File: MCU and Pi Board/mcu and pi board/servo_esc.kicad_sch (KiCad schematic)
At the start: 4 parts, among them J10 Conn_01x03_Pin, J11 Conn_01x03_Pin, J8 PWM Connector, J9 Conn_01x03_Pin

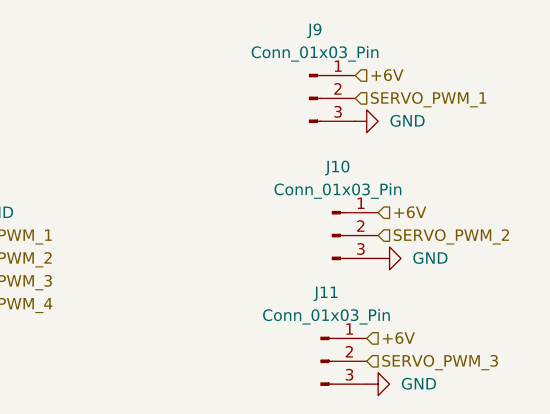
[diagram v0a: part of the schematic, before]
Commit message: added leds and minor fixes
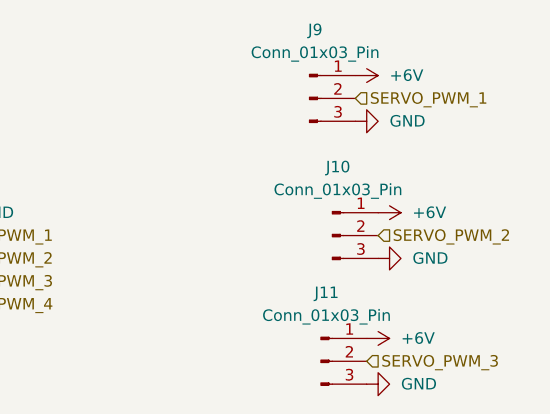
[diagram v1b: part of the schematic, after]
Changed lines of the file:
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@@
-		)
-	)
-	(hierarchical_label "+6V"
-		(shape input)
-		(at 165.1 49.53 0)
-		(effects
-			(font
-				(size 1.27 1.27)
-			)
-			(justify left)
 		)
 	)
@@
 		)
 	)
-	(hierarchical_label "+6V"
-		(shape input)
-		(at 167.64 64.77 0)
-		(effects
-			(font
-				(size 1.27 1.27)
-			)
-			(justify left)
-		)
-	)
 	(hierarchical_label "ESC_PWM_2"
 		(shape input)
@@
 		)
 	)
-	(hierarchical_label "+6V"
-		(shape input)
-		(at 166.37 78.74 0)
-		(effects
-			(font
-				(size 1.27 1.27)
-			)
-			(justify left)
-		)
-	)
 	(hierarchical_label "ESC_PWM_1"
 		(shape input)
@@
 	)
 	(symbol
+		(lib_id "power:+6V")
+		(at 165.1 49.53 270)
+		(unit 1)
+		(exclude_from_sim no)
+		(in_bom yes)
+		(on_board yes)
+		(dnp no)
+		(fields_autoplaced yes)
+		(property "Reference" "#PWR062"
+			(at 161.29 49.53 0)
+			(effects
+				(font
+					(size 1.27 1.27)
+				)
+				(hide yes)
+			)
+		)
+		(property "Value" "+6V"
+			(at 168.91 49.5299 90)
+			(effects
+				(font
+					(size 1.27 1.27)
+				)
+				(justify left)
+			)
+		)
+		(property "Footprint" ""
+			(at 165.1 49.53 0)
+			(effects
+				(font
+					(size 1.27 1.27)
+				)
+				(hide yes)
+			)
+		)
+		(property "Datasheet" ""
+			(at 165.1 49.53 0)
+			(effects
+				(font
+					(size 1.27 1.27)
+				)
+				(hide yes)
+			)
+		)
+		(property "Description" "Power symbol creates a global label with name \"+6V\""
+			(at 165.1 49.53 0)
+			(effects
+				(font
+					(size 1.27 1.27)
+				)
+				(hide yes)
+			)
+		)
+		(pin "1"
+		)
+		(instances
+			(project ""
+				(path "/b20a486a-db1b-4621-abfe-a5d205c676b3/cf9b13c4-ce92-4bbb-82dc-82851d7b76da"
+					(reference "#PWR062")
+					(unit 1)
+				)
+			)
+		)
+	)
+	(symbol
 		(lib_id "power:GND")
 		(at 93.98 67.31 270)
@@
 	)
 	(symbol
+		(lib_id "power:+6V")
+		(at 167.64 64.77 270)
+		(unit 1)
+		(exclude_from_sim no)
+		(in_bom yes)
+		(on_board yes)
+		(dnp no)
+		(fields_autoplaced yes)
+		(property "Reference" "#PWR063"
+			(at 163.83 64.77 0)
+			(effects
+				(font
+					(size 1.27 1.27)
+				)
+				(hide yes)
+			)
+		)
+		(property "Value" "+6V"
+			(at 171.45 64.7699 90)
+			(effects
+				(font
+					(size 1.27 1.27)
+				)
+				(justify left)
+			)
+		)
+		(property "Footprint" ""
+			(at 167.64 64.77 0)
+			(effects
+				(font
+					(size 1.27 1.27)
+				)
+				(hide yes)
+			)
+		)
+		(property "Datasheet" ""
+			(at 167.64 64.77 0)
+			(effects
+				(font
+					(size 1.27 1.27)
+				)
+				(hide yes)
+			)
+		)
+		(property "Description" "Power symbol creates a global label with name \"+6V\""
+			(at 167.64 64.77 0)
+			(effects
+				(font
+					(size 1.27 1.27)
+				)
+				(hide yes)
+			)
+		)
+		(pin "1"
+		)
+		(instances
+			(project "mcu and pi board"
+				(path "/b20a486a-db1b-4621-abfe-a5d205c676b3/cf9b13c4-ce92-4bbb-82dc-82851d7b76da"
+					(reference "#PWR063")
+					(unit 1)
+				)
+			)
+		)
+	)
+	(symbol
 		(lib_id "Connector:Conn_01x03_Pin")
 		(at 161.29 81.28 0)
@@
 					(unit 1)
 				)
+			)
+		)
+	)
+	(symbol
+		(lib_id "power:+6V")
+		(at 166.37 78.74 270)
+		(unit 1)
+		(exclude_from_sim no)
+		(in_bom yes)
+		(on_board yes)
+		(dnp no)
+		(fields_autoplaced yes)
+		(property "Reference" "#PWR064"
+			(at 162.56 78.74 0)
+			(effects
+				(font
+					(size 1.27 1.27)
+				)
+				(hide yes)
+			)
+		)
+		(property "Value" "+6V"
+			(at 170.18 78.7399 90)
+			(effects
+				(font
+					(size 1.27 1.27)
+				)
+				(justify left)
+			)
+		)
+		(property "Footprint" ""
+			(at 166.37 78.74 0)
+			(effects
+				(font
+					(size 1.27 1.27)
+				)
+				(hide yes)
+			)
+		)
+		(property "Datasheet" ""
+			(at 166.37 78.74 0)
+			(effects
+				(font
+					(size 1.27 1.27)
+				)
+				(hide yes)
+			)
+		)
+		(property "Description" "Power symbol creates a global label with name \"+6V\""
+			(at 166.37 78.74 0)
+			(effects
+				(font
+					(size 1.27 1.27)
+				)
+				(hide yes)
+			)
+		)
+		(pin "1"
+		)
+		(instances
+			(project "mcu and pi board"
+				(path "/b20a486a-db1b-4621-abfe-a5d205c676b3/cf9b13c4-ce92-4bbb-82dc-82851d7b76da"
+					(reference "#PWR064")
+					(unit 1)
+				)

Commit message: minor edits
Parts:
- added C8: 10u, symbol Device:C
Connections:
- net +12V: now also C8.1
- net GND: now also C8.2
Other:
- note added: "Add decoupling to servos"
- note added: "Add decoupling to thrusters"
- note added: "add tools c"
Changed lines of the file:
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@@
 	(generator_version "9.0")
 	(paper "A4")
+	(text "Add decoupling to servos"
+		(exclude_from_sim no)
+		(at 192.278 56.388 0)
+		(effects
+			(font
+				(size 1.27 1.27)
+			)
+		)
+	)
+	(text "add tools c"
+		(exclude_from_sim no)
+		(at 102.616 83.312 0)
+		(effects
+			(font
+				(size 1.27 1.27)
+			)
+		)
+	)
+	(text "Add decoupling to thrusters\n"
+		(exclude_from_sim no)
+		(at 104.648 53.848 0)
+		(effects
+			(font
+				(size 1.27 1.27)
+			)
+		)
+	)
+	(junction
+		(at 83.82 59.69)
+		(diameter 0)
+		(color 0 0 0 0)
+	)
+	(junction
+		(at 83.82 67.31)
+		(diameter 0)
+		(color 0 0 0 0)
+	)
+	(wire
+		(pts
+			(xy 91.44 59.69) (xy 91.44 64.77)
+		)
+		(stroke
+			(width 0)
+			(type default)
+		)
+	)
+	(wire
+		(pts
+			(xy 91.44 64.77) (xy 93.98 64.77)
+		)
+		(stroke
+			(width 0)
+			(type default)
+		)
+	)
+	(wire
+		(pts
+			(xy 82.55 67.31) (xy 83.82 67.31)
+		)
+		(stroke
+			(width 0)
+			(type default)
+		)
+	)
+	(wire
+		(pts
+			(xy 83.82 67.31) (xy 93.98 67.31)
+		)
+		(stroke
+			(width 0)
+			(type default)
+		)
+	)
+	(wire
+		(pts
+			(xy 83.82 59.69) (xy 91.44 59.69)
+		)
+		(stroke
+			(width 0)
+			(type default)
+		)
+	)
+	(wire
+		(pts
+			(xy 82.55 59.69) (xy 83.82 59.69)
+		)
+		(stroke
+			(width 0)
+			(type default)
+		)
+	)
 	(hierarchical_label "SERVO_PWM_3"
 		(shape input)
@@
 	(symbol
 		(lib_id "power:GND")
-		(at 93.98 67.31 270)
+		(at 82.55 67.31 270)
 		(unit 1)
 		(exclude_from_sim no)
@@
 		(fields_autoplaced yes)
 		(property "Reference" "#PWR032"
-			(at 87.63 67.31 0)
+			(at 76.2 67.31 0)
 			(effects
 				(font
@@
 		)
 		(property "Value" "GND"
-			(at 90.17 67.3099 90)
+			(at 78.74 67.3099 90)
 			(effects
 				(font
@@
 		)
 		(property "Footprint" ""
-			(at 93.98 67.31 0)
+			(at 82.55 67.31 0)
 			(effects
 				(font
@@
 		)
 		(property "Datasheet" ""
-			(at 93.98 67.31 0)
+			(at 82.55 67.31 0)
 			(effects
 				(font
@@
 		)
 		(property "Description" "Power symbol creates a global label with name \"GND\" , ground"
-			(at 93.98 67.31 0)
+			(at 82.55 67.31 0)
 			(effects
 				(font
@@
 	(symbol
 		(lib_id "power:+12V")
-		(at 93.98 64.77 90)
+		(at 82.55 59.69 90)
 		(unit 1)
 		(exclude_from_sim no)
@@
 		(fields_autoplaced yes)
 		(property "Reference" "#PWR031"
-			(at 97.79 64.77 0)
+			(at 86.36 59.69 0)
 			(effects
 				(font
@@
 		)
 		(property "Value" "+12V"
-			(at 90.17 64.7699 90)
+			(at 78.74 59.6899 90)
 			(effects
 				(font
@@
 		)
 		(property "Footprint" ""
-			(at 93.98 64.77 0)
+			(at 82.55 59.69 0)
 			(effects
 				(font
@@
 		)
 		(property "Datasheet" ""
-			(at 93.98 64.77 0)
+			(at 82.55 59.69 0)
 			(effects
 				(font
@@
 		)
 		(property "Description" "Power symbol creates a global label with name \"+12V\""
-			(at 93.98 64.77 0)
+			(at 82.55 59.69 0)
 			(effects
 				(font
@@
 					(unit 1)
 				)
+			)
+		)
+	)
+	(symbol
+		(lib_id "Device:C")
+		(at 83.82 63.5 0)
+		(unit 1)
+		(exclude_from_sim no)
+		(in_bom yes)
+		(on_board yes)
+		(dnp no)
+		(fields_autoplaced yes)
+		(property "Reference" "C8"
+			(at 87.63 62.2299 0)
+			(effects
+				(font
+					(size 1.27 1.27)
+				)
+				(justify left)
+			)
+		)
+		(property "Value" "10u"
+			(at 87.63 64.7699 0)
+			(effects
+				(font
+					(size 1.27 1.27)
+				)
+				(justify left)
+			)
+		)
+		(property "Footprint" ""
+			(at 84.7852 67.31 0)
+			(effects
+				(font
+					(size 1.27 1.27)
+				)
+				(hide yes)
+			)
+		)
+		(property "Datasheet" "~"
+			(at 83.82 63.5 0)
+			(effects
+				(font
+					(size 1.27 1.27)
+				)
+				(hide yes)
+			)
+		)
+		(property "Description" "Unpolarized capacitor"
+			(at 83.82 63.5 0)
+			(effects
+				(font
+					(size 1.27 1.27)
+				)
+				(hide yes)
+			)
+		)
+		(pin "1"
+		)
+		(pin "2"
+		)
+		(instances
+			(project ""
+				(path "/b20a486a-db1b-4621-abfe-a5d205c676b3/cf9b13c4-ce92-4bbb-82dc-82851d7b76da"
+					(reference "C8")
+					(unit 1)
+				)

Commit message: pretty much done i think
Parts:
- added C10, C22, C23, C24, C25: 1000u, symbol Device:C
- added C17: 1u, symbol Device:C
- added C20, C21, C9: 0.1u, symbol Device:C
- added R10, R17, R9: 100, symbol Device:R_US
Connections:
- net +12V: now also C23.1, C24.1, C25.1
- net +6V: now also C10.1, C17.1, C22.1
- net GND: now also C10.2, C17.2, C20.2, C21.2, C22.2, C23.2, C24.2, C25.2, C9.2
- net SERVO_PWM_1: now also R9.2; no longer J9.2 (Pin_2)
- net SERVO_PWM_2: now also R10.2; no longer J10.2 (Pin_2)
- net SERVO_PWM_3: now also R17.2; no longer J11.2 (Pin_2)
- new net: C20.1, J10.2 (Pin_2), R10.1
- new net: C21.1, J11.2 (Pin_2), R17.1
- new net: C9.1, J9.2 (Pin_2), R9.1
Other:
- note added: "buffer current spikes"
- note added: "filter high frequency"
- note removed: "add tools c"
- moved on the sheet: C8, J10, J11, J9

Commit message: pretty much done
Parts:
- added J22: Conn_01x03_Pin, symbol Connector:Conn_01x03_Pin
- added U6, U7: MC74HC157ADR2G, SOIC-16_ONS, symbol custom library:MC74HC157ADR2G
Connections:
- net SERVO_PWM_3 is gone; now on net SERVO_PWM_2: R17.2
- net +5V: now also J22.1 (Pin_1), U6.16 (VCC), U7.16 (VCC)
- net ESC_PWM_1: now also U6.7 (Y1)
- net ESC_PWM_2: now also U6.9 (Y2)
- net ESC_PWM_3: now also U6.12 (Y3)
- net GND: now also J22.3 (Pin_3), U6.15 (OUTPUTENABLE), U6.8 (GND), U7.15 (OUTPUTENABLE), U7.8 (GND)
- net SERVO_PWM_1: now also R10.2, U7.7 (Y1); no longer R9.2
- net SERVO_PWM_2: now also U7.9 (Y2); no longer R10.2
- new net ESC_PWM_0: U6.4 (Y0)
- new net RP2350B_ESC_PWM_0: U6.3 (B0)
- new net RP2350B_ESC_PWM_1: U6.6 (B1)
- new net RP2350B_ESC_PWM_2: U6.10 (B2)
- new net RP2350B_ESC_PWM_3: U6.13 (B3)
- new net RP2350B_SERVO_PWM_0: U7.3 (B0)
- new net RP2350B_SERVO_PWM_1: U7.6 (B1)
- new net RP2350B_SERVO_PWM_2: U7.10 (B2)
- new net SEL: J22.2 (Pin_2), U6.1 (SELECT), U7.1 (SELECT)
- new net SERVO_PWM_0: R9.2, U7.4 (Y0)
- new net STM_ESC_PWM_0: U6.2 (A0)
- new net STM_ESC_PWM_1: U6.5 (A1)
- new net STM_ESC_PWM_2: U6.11 (A2)
- new net STM_ESC_PWM_3: U6.14 (A3)
- new net STM_SERVO_PWM_0: U7.2 (A0)
- new net STM_SERVO_PWM_1: U7.5 (A1)
- new net STM_SERVO_PWM_2: U7.11 (A2)
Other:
- note removed: "Add decoupling to servos"
- note removed: "Add decoupling to thrusters"

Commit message: started routing
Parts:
- removed C10: 1000u, symbol Device:C
- removed C20, C21, C9: 0.1u, symbol Device:C
- removed J10, J11, J9: Conn_01x03_Pin, symbol Connector:Conn_01x03_Pin
- removed R10, R17, R9: 100, symbol Device:R_US
- added C26, C39: 0.1u, Capacitor_SMD:C_0603_1608Metric_Pad1.08x0.95mm_HandSolder, symbol Device:C
- added C27, C40: 10u, Capacitor_SMD:C_0805_2012Metric_Pad1.18x1.45mm_HandSolder, symbol Device:C
- added J23, J24, J25: TB006-508-03BE, custom library:CUI_TB006-508-03BE, symbol custom library:TB006-508-03BE
- added J9: ESC ADAPTER - BACKPLANE, custom library:ESC Adapter - Backplane, symbol custom library:IPBT-105-H1-T-D-GP
- C17: value 1u -> 0.1u; footprint (none) -> Capacitor_SMD:C_0603_1608Metric_Pad1.08x0.95mm_HandSolder
- C22, C24: value 1000u -> 10u; footprint (none) -> Capacitor_SMD:C_0805_2012Metric_Pad1.18x1.45mm_HandSolder
- C23, C25: value 1000u -> 0.1u; footprint (none) -> Capacitor_SMD:C_0603_1608Metric_Pad1.08x0.95mm_HandSolder
- C8: footprint (none) -> Capacitor_SMD:C_0805_2012Metric_Pad1.18x1.45mm_HandSolder
- J22: footprint (none) -> Connector_PinHeader_2.54mm:PinHeader_1x03_P2.54mm_Vertical
- J8: footprint Custom:PWM, 12V, GND JST Connector -> custom library:PWM, 12V, GND JST Connector
- U6, U7: footprint SOIC-16_ONS -> custom library:SOIC-16_ONS
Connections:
- net ESC_PWM_0 is gone; now on net ESC_PWM_1: U6.4 (Y0)
- net +12V: now also C26.1, J9.04, J9.05, J9.09, J9.10, J9.11, J9.21, J9.22, J9.23, J9.26, J9.27, J9.28; no longer C25.1
- net +5V: now also J9.12
- net +6V: now also C25.1, C27.1, C39.1, C40.1, J23.1, J24.1, J25.1
- net ESC_PWM_1: now also J9.16; no longer U6.7 (Y1)
- net ESC_PWM_2: now also U6.7 (Y1), J9.19; no longer U6.9 (Y2)
- net ESC_PWM_3: now also U6.9 (Y2), J9.15; no longer U6.12 (Y3)
- net ESC_PWM_4: now also U6.12 (Y3), J9.17
- net ESC_Telemetry: now also J9.14
- net GND: now also C26.2, C27.2, C39.2, C40.2, J23.3, J24.3, J25.3, J9.01, J9.02, J9.03, J9.06, J9.07, J9.08, J9.13, J9.20, J9.24, J9.25, J9.29, J9.30
- net SERVO_PWM_0: now also J23.2
- net SERVO_PWM_1: now also J24.2
- net SERVO_PWM_2: now also J25.2
- no-connect marks 0 -> 1
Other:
- note removed: "buffer current spikes"
- note removed: "filter high frequency"

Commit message: yeet
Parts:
- added J29: Conn_02x02_Pin, Connector_PinSocket_2.54mm:PinSocket_2x02_P2.54mm_Vertical, symbol Connector_Generic:Conn_02x02_Odd_Even
- added J5: Conn_01x03_Pin, Connector_PinSocket_2.54mm:PinSocket_1x03_P2.54mm_Vertical, symbol Connector:Conn_01x03_Pin
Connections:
- net ESC_PWM_1: now also J29.1 (Pin_1)
- net ESC_PWM_2: now also J29.3 (Pin_3)
- net ESC_PWM_3: now also J29.4 (Pin_4)
- net ESC_PWM_4: now also J29.2 (Pin_2)
- net SERVO_PWM_0: now also J5.1 (Pin_1)
- net SERVO_PWM_1: now also J5.2 (Pin_2)
- net SERVO_PWM_2: now also J5.3 (Pin_3)
- no-connect marks 1 -> 4
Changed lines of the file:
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@@
+	)
+	(no_connect
+		(at 127 86.36)
 	)
 	(no_connect
 		(at 226.06 120.65)
 	)
+	(no_connect
+		(at 127 83.82)
+	)
+	(no_connect
+		(at 127 88.9)
+	)
 	(wire
 		(pts
@@
 		)
 	)
+	(label "SERVO_PWM_0"
+		(at 96.52 118.11 0)
+		(effects
+			(font
+				(size 1.27 1.27)
+			)
+			(justify left bottom)
+		)
+	)
+	(label "SERVO_PWM_2"
+		(at 96.52 123.19 0)
+		(effects
+			(font
+				(size 1.27 1.27)
+			)
+			(justify left bottom)
+		)
+	)
 	(label "ESC_PWM_4"
 		(at 271.78 74.93 0)
@@
 		)
 	)
+	(label "SERVO_PWM_1"
+		(at 96.52 120.65 0)
+		(effects
+			(font
+				(size 1.27 1.27)
+			)
+			(justify left bottom)
+		)
+	)
 	(label "ESC_PWM_2"
 		(at 226.06 123.19 0)
@@
 		)
 	)
+	(label "ESC_PWM_4"
+		(at 80.01 132.08 0)
+		(effects
+			(font
+				(size 1.27 1.27)
+			)
+			(justify left bottom)
+		)
+	)
 	(label "SERVO_PWM_0"
 		(at 66.04 86.36 180)
@@
 	(label "ESC_PWM_2"
 		(at 271.78 69.85 0)
+		(effects
+			(font
+				(size 1.27 1.27)
+			)
+			(justify left bottom)
+		)
+	)
+	(label "ESC_PWM_2"
+		(at 67.31 134.62 180)
+		(effects
+			(font
+				(size 1.27 1.27)
+			)
+			(justify right bottom)
+		)
+	)
+	(label "ESC_PWM_1"
+		(at 67.31 132.08 180)
+		(effects
+			(font
+				(size 1.27 1.27)
+			)
+			(justify right bottom)
+		)
+	)
+	(label "ESC_PWM_3"
+		(at 80.01 134.62 0)
 		(effects
 			(font
@@
 			)
 			(justify left)
+		)
+	)
+	(symbol
+		(lib_id "Connector_Generic:Conn_02x02_Odd_Even")
+		(at 72.39 132.08 0)
+		(unit 1)
+		(exclude_from_sim no)
+		(in_bom yes)
+		(on_board yes)
+		(dnp no)
+		(fields_autoplaced yes)
+		(property "Reference" "J29"
+			(at 73.66 125.73 0)
+			(effects
+				(font
+					(size 1.27 1.27)
+				)
+			)
+		)
+		(property "Value" "Conn_02x02_Pin"
+			(at 73.66 128.27 0)
+			(effects
+				(font
+					(size 1.27 1.27)
+				)
+			)
+		)
+		(property "Footprint" "Connector_PinSocket_2.54mm:PinSocket_2x02_P2.54mm_Vertical"
+			(at 72.39 132.08 0)
+			(effects
+				(font
+					(size 1.27 1.27)
+				)
+				(hide yes)
+			)
+		)
+		(property "Datasheet" "~"
+			(at 72.39 132.08 0)
+			(effects
+				(font
+					(size 1.27 1.27)
+				)
+				(hide yes)
+			)
+		)
+		(property "Description" "Generic connector, double row, 02x02, odd/even pin numbering scheme (row 1 odd numbers, row 2 even numbers), script generated (kicad-library-utils/schlib/autogen/connector/)"
+			(at 72.39 132.08 0)
+			(effects
+				(font
+					(size 1.27 1.27)
+				)
+				(hide yes)
+			)
+		)
+		(pin "1"
+		)
+		(pin "2"
+		)
+		(pin "3"
+		)
+		(pin "4"
+		)
+		(instances
+			(project "mcu and pi board"
+				(path "/b20a486a-db1b-4621-abfe-a5d205c676b3/cf9b13c4-ce92-4bbb-82dc-82851d7b76da"
+					(reference "J29")
+					(unit 1)
+				)
+			)
 		)
 	)
@@
 					(unit 1)
 				)
+			)
+		)
+	)
+	(symbol
+		(lib_id "Connector:Conn_01x03_Pin")
+		(at 91.44 120.65 0)
+		(unit 1)
+		(exclude_from_sim no)
+		(in_bom yes)
+		(on_board yes)
+		(dnp no)
+		(fields_autoplaced yes)
+		(property "Reference" "J5"
+			(at 92.075 113.03 0)
+			(effects
+				(font
+					(size 1.27 1.27)
+				)
+			)
+		)
+		(property "Value" "Conn_01x03_Pin"
+			(at 92.075 115.57 0)
+			(effects
+				(font
+					(size 1.27 1.27)
+				)
+			)
+		)
+		(property "Footprint" "Connector_PinSocket_2.54mm:PinSocket_1x03_P2.54mm_Vertical"
+			(at 91.44 120.65 0)
+			(effects
+				(font
+					(size 1.27 1.27)
+				)
+				(hide yes)
+			)
+		)
+		(property "Datasheet" "~"
+			(at 91.44 120.65 0)
+			(effects
+				(font
+					(size 1.27 1.27)
+				)
+				(hide yes)
+			)
+		)
+		(property "Description" "Generic connector, single row, 01x03, script generated"
+			(at 91.44 120.65 0)
+			(effects
+				(font
+					(size 1.27 1.27)
+				)
+				(hide yes)
+			)
+		)
+		(pin "1"
+		)
+		(pin "2"
+		)
+		(pin "3"
+		)
+		(instances
+			(project ""
+				(path "/b20a486a-db1b-4621-abfe-a5d205c676b3/cf9b13c4-ce92-4bbb-82dc-82851d7b76da"
+					(reference "J5")
+					(unit 1)
+				)
